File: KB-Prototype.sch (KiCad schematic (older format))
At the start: 44 parts

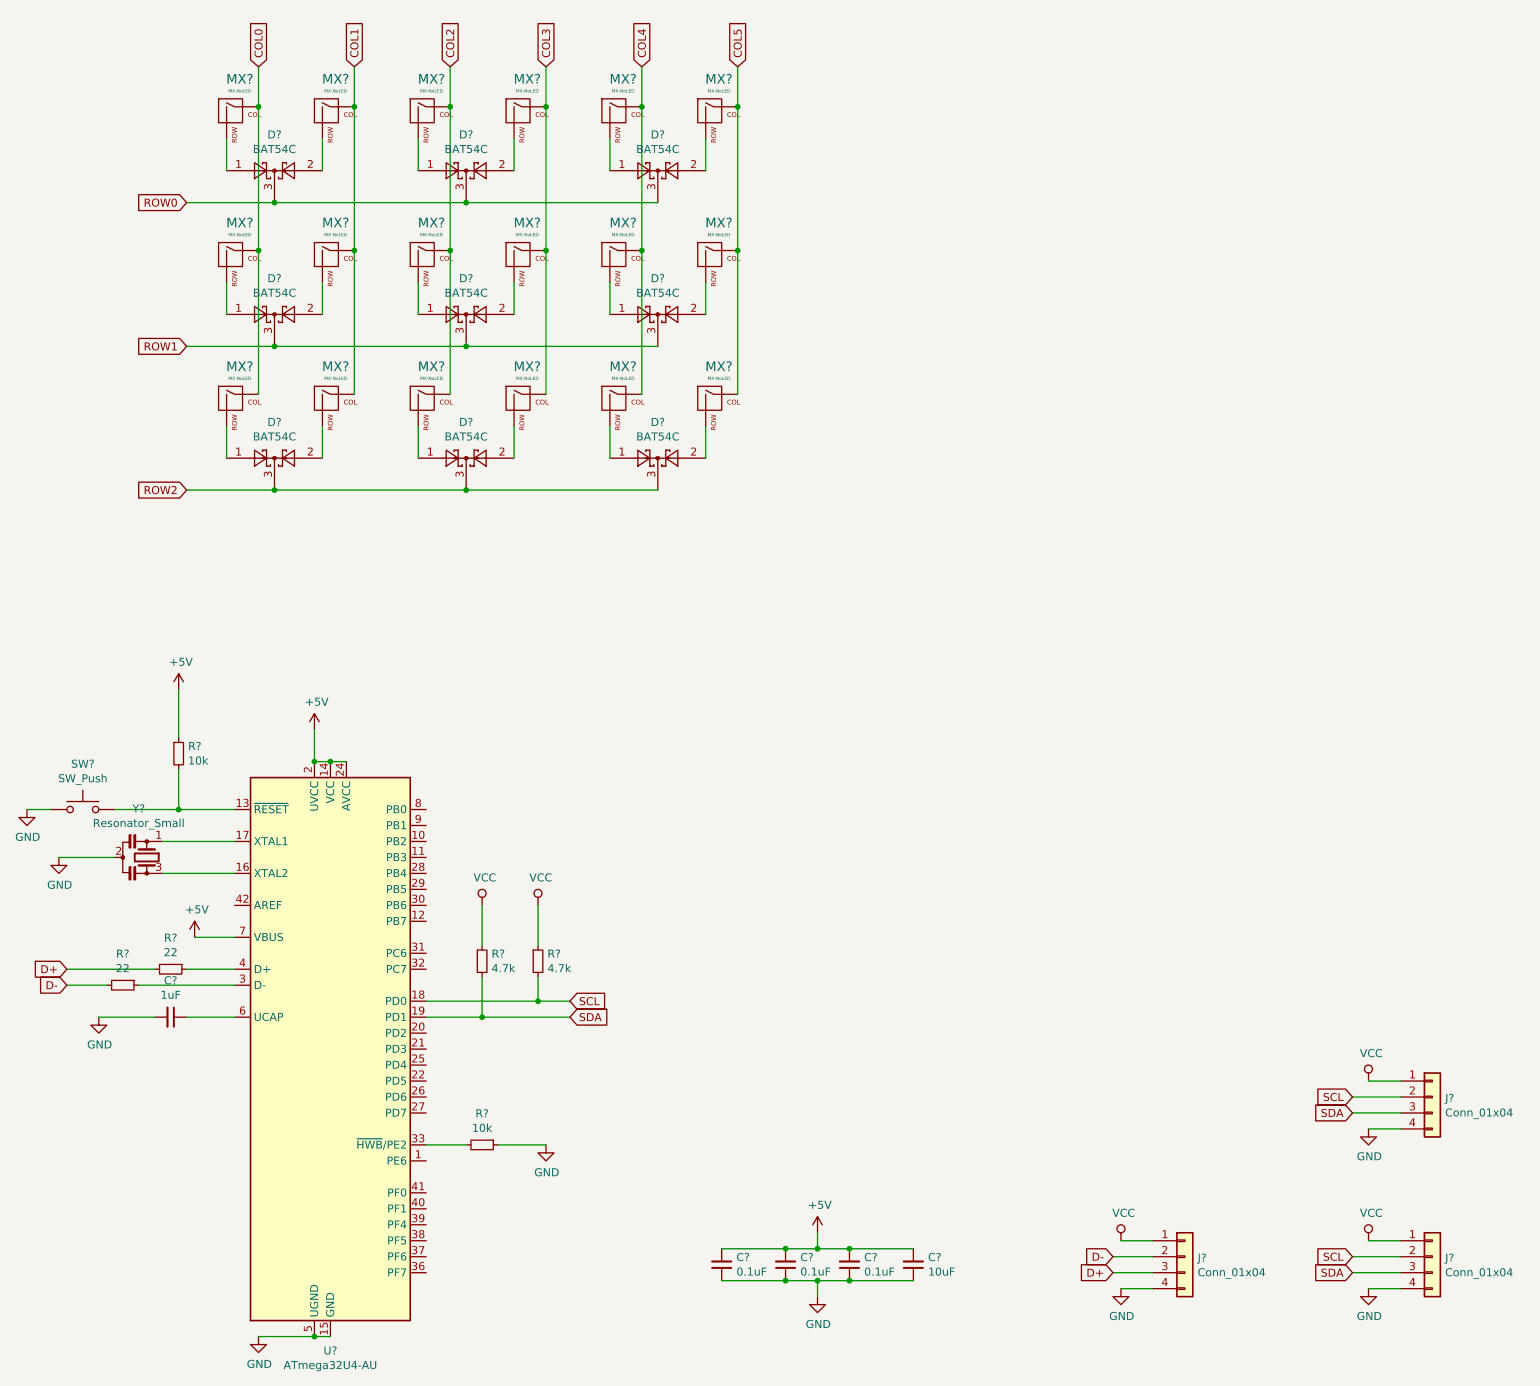
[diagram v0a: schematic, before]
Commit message: assigned footprints for components
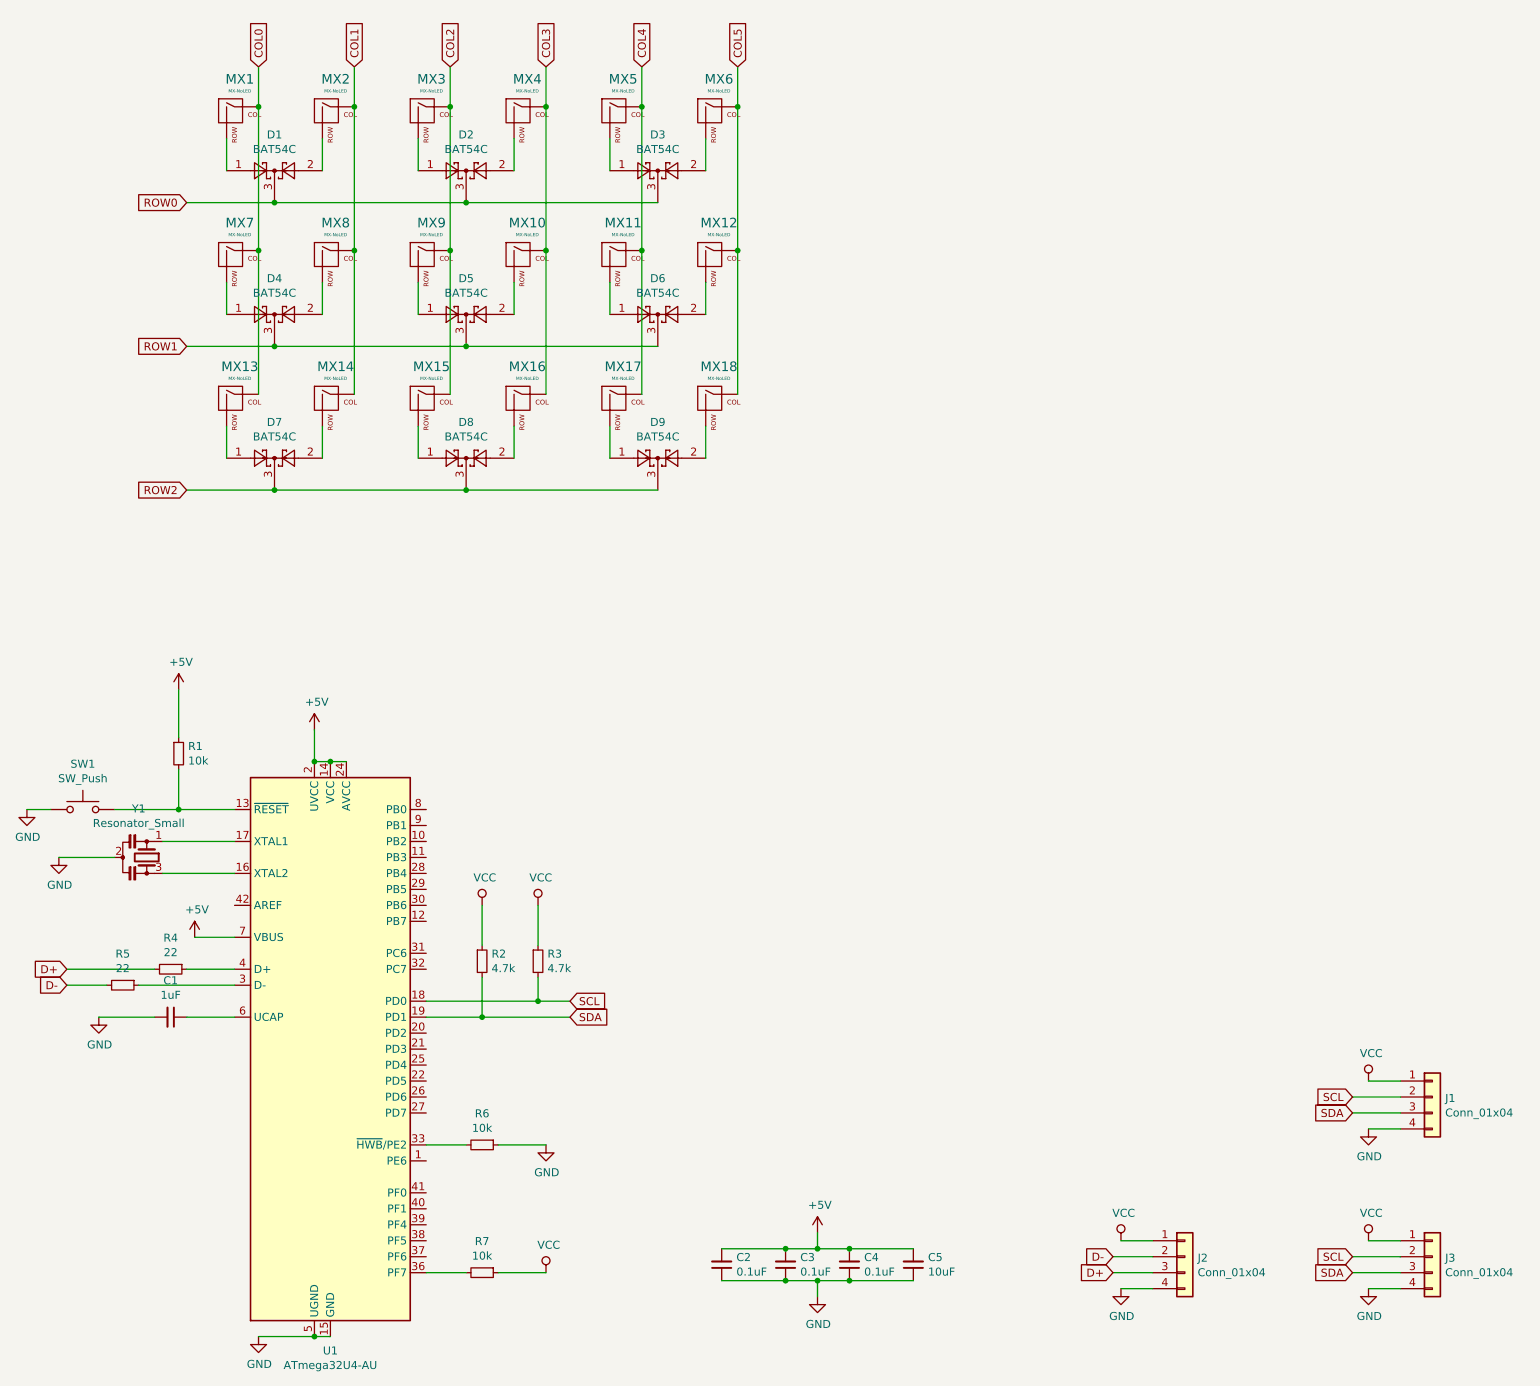
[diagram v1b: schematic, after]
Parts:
- added R7: 10k, Resistor_SMD:R_0805_2012Metric, symbol Device:R_Small
- C1, C2, C3, C4, C5: renamed from C?; footprint (none) -> Capacitor_SMD:C_0805_2012Metric
- J1, J2, J3: renamed from J?; footprint (none) -> random-keyboard-parts:JST-SR-4
- MX1, MX10, MX11, MX12, MX13, MX14, MX15, MX16, MX17, MX18, MX2, MX3, MX4, MX5, MX6, MX7, MX8, MX9: renamed from MX?; footprint (none) -> MX_Only:MXOnly-1U-NoLED
- R1, R2, R3, R4, R5, R6: renamed from R?; footprint (none) -> Resistor_SMD:R_0805_2012Metric
- SW1: renamed from SW?; footprint (none) -> random-keyboard-parts:SKQG-1155865
- Y1: renamed from Y?; footprint (none) -> DIMR_Keyboard_Parts:CSTCE
- gave numbers to parts that had none: 10
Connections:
- net VCC: now also R7.1
- net at U1.36 (PF7): now also R7.2

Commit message: pcb routed, except rows/cols
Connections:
- net VCC is gone; now on net +5V: J1.1 (Pin_1), J2.1 (Pin_1), J3.1 (Pin_1), R2.1, R3.1, R7.1
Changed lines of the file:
@@
 Wire Wire Line
 	3700 8300 3350 8300
-$Comp
-L power:VCC #PWR0111
-U 1 1 5F0C30FA
-P 3700 7600
-F 0 "#PWR0111" H 3700 7450 50  0001 C CNN
-F 1 "VCC" H 3717 7773 50  0000 C CNN
-F 2 "" H 3700 7600 50  0001 C CNN
-F 3 "" H 3700 7600 50  0001 C CNN
-	1    3700 7600
-	1    0    0    -1
-$EndComp
-$Comp
-L power:VCC #PWR0112
-U 1 1 5F0C389A
-P 4050 7600
-F 0 "#PWR0112" H 4050 7450 50  0001 C CNN
-F 1 "VCC" H 4067 7773 50  0000 C CNN
-F 2 "" H 4050 7600 50  0001 C CNN
-F 3 "" H 4050 7600 50  0001 C CNN
-	1    4050 7600
-	1    0    0    -1
-$EndComp
 Wire Wire Line
 	3700 7850 3700 7600
@@
 Wire Wire Line
 	7900 9900 7650 9900
-$Comp
-L power:VCC #PWR0113
-U 1 1 5F0CF68B
-P 7700 9700
-F 0 "#PWR0113" H 7700 9550 50  0001 C CNN
-F 1 "VCC" H 7717 9873 50  0000 C CNN
-F 2 "" H 7700 9700 50  0001 C CNN
-F 3 "" H 7700 9700 50  0001 C CNN
-	1    7700 9700
-	1    0    0    -1
-$EndComp
 Wire Wire Line
 	7900 9700 7700 9700
@@
 Wire Wire Line
 	9450 9900 9150 9900
-$Comp
-L power:VCC #PWR0115
-U 1 1 5F0D747F
-P 9250 9700
-F 0 "#PWR0115" H 9250 9550 50  0001 C CNN
-F 1 "VCC" H 9267 9873 50  0000 C CNN
-F 2 "" H 9250 9700 50  0001 C CNN
-F 3 "" H 9250 9700 50  0001 C CNN
-	1    9250 9700
-	1    0    0    -1
-$EndComp
 Wire Wire Line
 	9450 9700 9250 9700
@@
 Wire Wire Line
 	9450 8900 9150 8900
-$Comp
-L power:VCC #PWR0117
-U 1 1 5F0DC514
-P 9250 8700
-F 0 "#PWR0117" H 9250 8550 50  0001 C CNN
-F 1 "VCC" H 9267 8873 50  0000 C CNN
-F 2 "" H 9250 8700 50  0001 C CNN
-F 3 "" H 9250 8700 50  0001 C CNN
-	1    9250 8700
-	1    0    0    -1
-$EndComp
 Wire Wire Line
 	9450 8700 9250 8700
@@
 ROW2
 $Comp
-L power:VCC #PWR0119
-U 1 1 5F1767C0
-P 4100 9900
-F 0 "#PWR0119" H 4100 9750 50  0001 C CNN
-F 1 "VCC" H 4117 10073 50  0000 C CNN
-F 2 "" H 4100 9900 50  0001 C CNN
-F 3 "" H 4100 9900 50  0001 C CNN
-	1    4100 9900
-	1    0    0    -1
-$EndComp
-$Comp
 L Device:R_Small R7
 U 1 1 5F1774D5
@@
 Wire Wire Line
 	3600 9900 3350 9900
+$Comp
+L power:+5V #PWR0111
+U 1 1 5F1EA5F6
+P 4050 7600
+F 0 "#PWR0111" H 4050 7450 50  0001 C CNN
+F 1 "+5V" H 4065 7773 50  0000 C CNN
+F 2 "" H 4050 7600 50  0001 C CNN
+F 3 "" H 4050 7600 50  0001 C CNN
+	1    4050 7600
+	1    0    0    -1
+$EndComp
+$Comp
+L power:+5V #PWR0112
+U 1 1 5F1EB1C4
+P 3700 7600
+F 0 "#PWR0112" H 3700 7450 50  0001 C CNN
+F 1 "+5V" H 3715 7773 50  0000 C CNN
+F 2 "" H 3700 7600 50  0001 C CNN
+F 3 "" H 3700 7600 50  0001 C CNN
+	1    3700 7600
+	1    0    0    -1
+$EndComp
+$Comp
+L power:+5V #PWR0113
+U 1 1 5F1EBE36
+P 9250 8700
+F 0 "#PWR0113" H 9250 8550 50  0001 C CNN
+F 1 "+5V" H 9265 8873 50  0000 C CNN
+F 2 "" H 9250 8700 50  0001 C CNN
+F 3 "" H 9250 8700 50  0001 C CNN
+	1    9250 8700
+	1    0    0    -1
+$EndComp
+$Comp
+L power:+5V #PWR0115
+U 1 1 5F1EC424
+P 9250 9700
+F 0 "#PWR0115" H 9250 9550 50  0001 C CNN
+F 1 "+5V" H 9265 9873 50  0000 C CNN
+F 2 "" H 9250 9700 50  0001 C CNN
+F 3 "" H 9250 9700 50  0001 C CNN
+	1    9250 9700
+	1    0    0    -1
+$EndComp
+$Comp
+L power:+5V #PWR0117
+U 1 1 5F1EC966
+P 7700 9700
+F 0 "#PWR0117" H 7700 9550 50  0001 C CNN
+F 1 "+5V" H 7715 9873 50  0000 C CNN
+F 2 "" H 7700 9700 50  0001 C CNN
+F 3 "" H 7700 9700 50  0001 C CNN
+	1    7700 9700
+	1    0    0    -1
+$EndComp
+$Comp
+L power:+5V #PWR?
+U 1 1 5F1F959F
+P 4100 9900
+F 0 "#PWR?" H 4100 9750 50  0001 C CNN
+F 1 "+5V" H 4115 10073 50  0000 C CNN
+F 2 "" H 4100 9900 50  0001 C CNN
+F 3 "" H 4100 9900 50  0001 C CNN
+	1    4100 9900
+	1    0    0    -1
+$EndComp
 $EndSCHEMATC

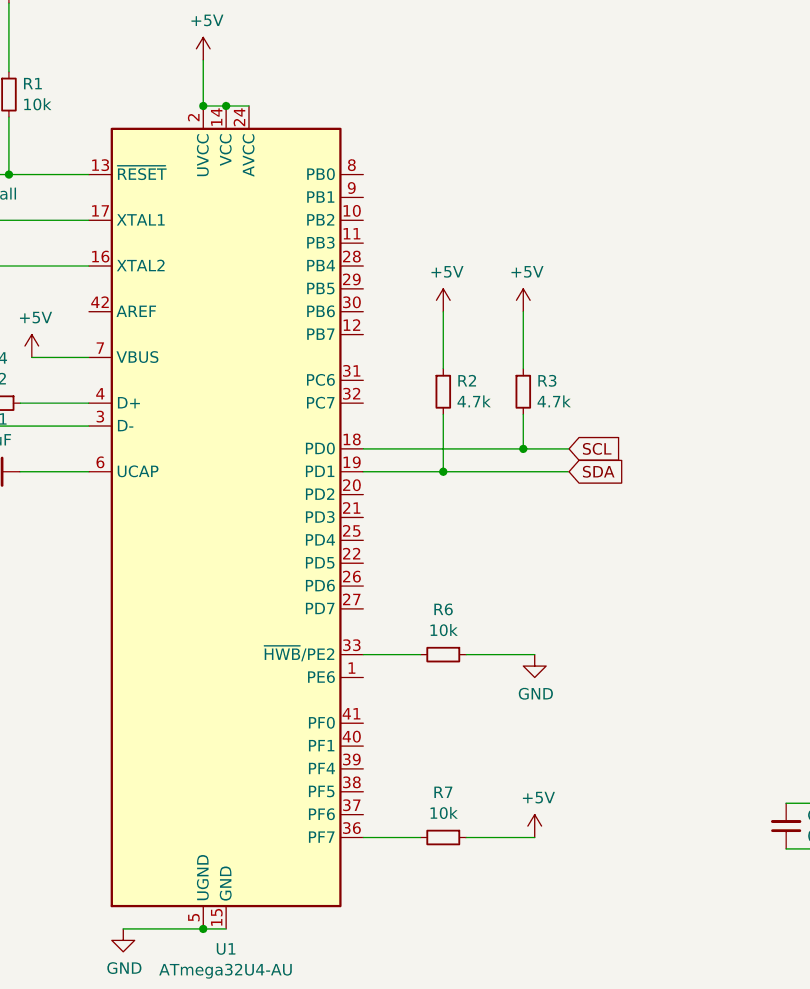
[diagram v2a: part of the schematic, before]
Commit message: hooked up cols/row, added silkscreen
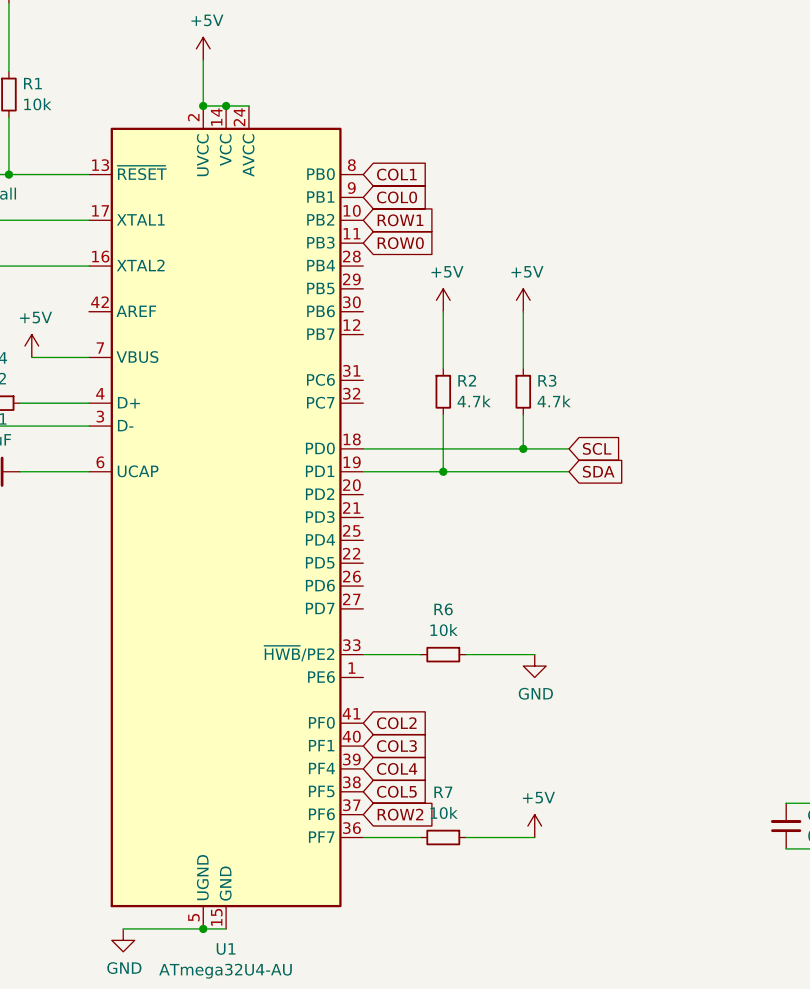
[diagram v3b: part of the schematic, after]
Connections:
- net COL0: now also U1.9 (PB1)
- net COL1: now also U1.8 (PB0)
- net COL2: now also U1.41 (PF0)
- net COL3: now also U1.40 (PF1)
- net COL4: now also U1.39 (PF4)
- net COL5: now also U1.38 (PF5)
- net ROW0: now also U1.11 (PB3)
- net ROW1: now also U1.10 (PB2)
- net ROW2: now also U1.37 (PF6)
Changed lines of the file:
@@
 EESchema Schematic File Version 4
+LIBS:KB-Prototype-cache
 EELAYER 29 0
 EELAYER END
@@
 $EndComp
 $Comp
-L power:+5V #PWR?
+L power:+5V #PWR0119
 U 1 1 5F1F959F
 P 4100 9900
-F 0 "#PWR?" H 4100 9750 50  0001 C CNN
+F 0 "#PWR0119" H 4100 9750 50  0001 C CNN
 F 1 "+5V" H 4115 10073 50  0000 C CNN
 F 2 "" H 4100 9900 50  0001 C CNN
@@
 	1    0    0    -1
 $EndComp
+Text GLabel 3350 7300 2    50   Input ~ 0
+ROW0
+Text GLabel 3350 7200 2    50   Input ~ 0
+ROW1
+Text GLabel 3350 7100 2    50   Input ~ 0
+COL0
+Text GLabel 3350 7000 2    50   Input ~ 0
+COL1
+Text GLabel 3350 9400 2    50   Input ~ 0
+COL2
+Text GLabel 3350 9500 2    50   Input ~ 0
+COL3
+Text GLabel 3350 9600 2    50   Input ~ 0
+COL4
+Text GLabel 3350 9700 2    50   Input ~ 0
+COL5
+Text GLabel 3350 9800 2    50   Input ~ 0
+ROW2
 $EndSCHEMATC

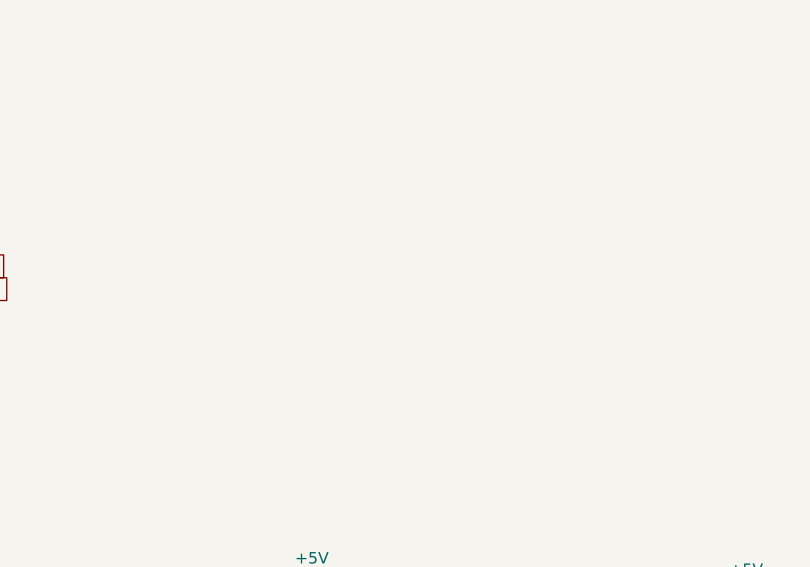
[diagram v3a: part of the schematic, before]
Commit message: added mounting holes
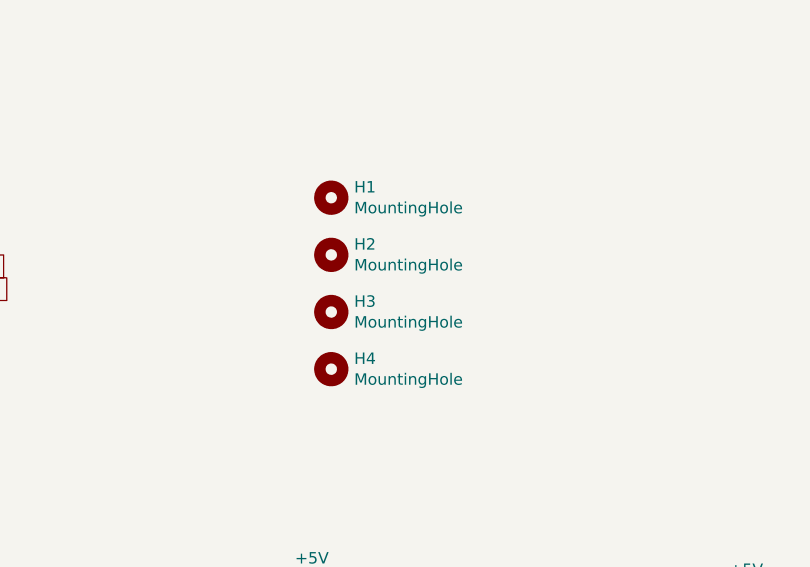
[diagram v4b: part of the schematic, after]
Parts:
- added H1, H2, H3, H4: MountingHole, random-keyboard-parts:Generic-Mounthole, symbol Mechanical:MountingHole
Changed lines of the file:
@@
 Text GLabel 3350 9800 2    50   Input ~ 0
 ROW2
+$Comp
+L Mechanical:MountingHole H1
+U 1 1 5F0A61CC
+P 5900 7900
+F 0 "H1" H 6000 7946 50  0000 L CNN
+F 1 "MountingHole" H 6000 7855 50  0000 L CNN
+F 2 "random-keyboard-parts:Generic-Mounthole" H 5900 7900 50  0001 C CNN
+F 3 "~" H 5900 7900 50  0001 C CNN
+	1    5900 7900
+	1    0    0    -1
+$EndComp
+$Comp
+L Mechanical:MountingHole H2
+U 1 1 5F0A65F2
+P 5900 8150
+F 0 "H2" H 6000 8196 50  0000 L CNN
+F 1 "MountingHole" H 6000 8105 50  0000 L CNN
+F 2 "random-keyboard-parts:Generic-Mounthole" H 5900 8150 50  0001 C CNN
+F 3 "~" H 5900 8150 50  0001 C CNN
+	1    5900 8150
+	1    0    0    -1
+$EndComp
+$Comp
+L Mechanical:MountingHole H3
+U 1 1 5F0A6A00
+P 5900 8400
+F 0 "H3" H 6000 8446 50  0000 L CNN
+F 1 "MountingHole" H 6000 8355 50  0000 L CNN
+F 2 "random-keyboard-parts:Generic-Mounthole" H 5900 8400 50  0001 C CNN
+F 3 "~" H 5900 8400 50  0001 C CNN
+	1    5900 8400
+	1    0    0    -1
+$EndComp
+$Comp
+L Mechanical:MountingHole H4
+U 1 1 5F0A6CB7
+P 5900 8650
+F 0 "H4" H 6000 8696 50  0000 L CNN
+F 1 "MountingHole" H 6000 8605 50  0000 L CNN
+F 2 "random-keyboard-parts:Generic-Mounthole" H 5900 8650 50  0001 C CNN
+F 3 "~" H 5900 8650 50  0001 C CNN
+	1    5900 8650
+	1    0    0    -1
+$EndComp
 $EndSCHEMATC
